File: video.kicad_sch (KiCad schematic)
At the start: 4 parts, among them J2 Board Interconnect Female, J2 Video Output Female, J3 Conn_02x08_Odd_Even

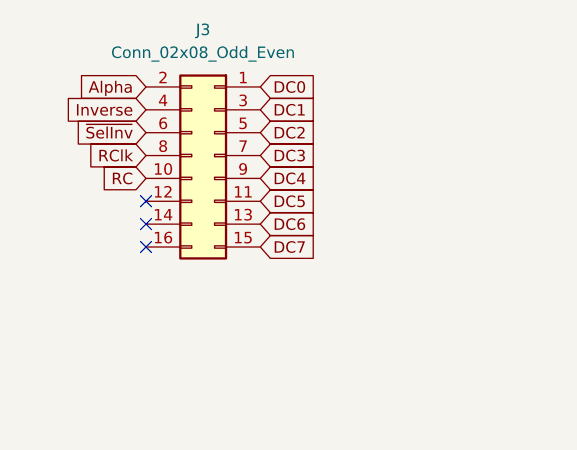
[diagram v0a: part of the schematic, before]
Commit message: reinforce power rails
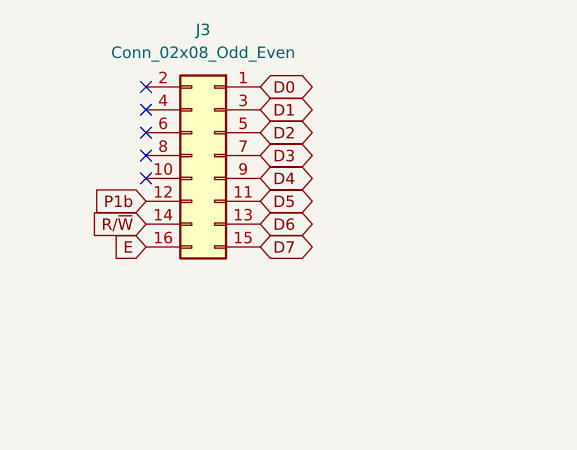
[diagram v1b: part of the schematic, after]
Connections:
- net P1b: now reaches J3.12 (Pin_12)
- net R/~{W}: now reaches J3.14 (Pin_14)
- net E: now reaches J3.16 (Pin_16)
- net Alpha: no longer names the net of J3.2 (Pin_2)
- net DC0 renamed D0
- net DC1 renamed D1
- net DC2 renamed D2
- net DC3 renamed D3
- net DC4 renamed D4
- net DC5 renamed D5
- net DC6 renamed D6
- net DC7 renamed D7
- net Inverse: no longer names the net of J3.4 (Pin_4)
- net RC: no longer names the net of J3.10 (Pin_10)
- net RClk: no longer names the net of J3.8 (Pin_8)
- net ~{SelInv}: no longer names the net of J3.6 (Pin_6)
- no-connect marks 5 -> 7
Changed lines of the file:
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@@
     (comment 2 "Reposition dram and buffer")
   )
-  (no_connect (at 123.19 116.84))
-  (no_connect (at 123.19 121.92))
-  (no_connect (at 123.19 119.38))
+  (no_connect (at 123.19 111.76))
+  (no_connect (at 123.19 114.3))
+  (no_connect (at 123.19 104.14))
+  (no_connect (at 123.19 106.68))
   (no_connect (at 137.1092 165.4048))
   (no_connect (at 124.4092 190.8048))
+  (no_connect (at 123.19 109.22))
   (global_label "DO5" (shape input) (at 124.4092 180.6448 180) (fields_autoplaced)
     (effects (font (size 1.27 1.27)) (justify right))
     (property "Intersheetrefs" "${INTERSHEET_REFS}" (at 118.3476 180.6448 0)
+      (effects (font (size 1.27 1.27)) (justify right) hide)
+    )
+  )
+  (global_label "D6" (shape bidirectional) (at 135.89 119.38 0) (fields_autoplaced)
+    (effects (font (size 1.27 1.27)) (justify left))
+    (property "Intersheetrefs" "${INTERSHEET_REFS}" (at 140.6937 119.3006 0)
+      (effects (font (size 1.27 1.27)) (justify left) hide)
+    )
+  )
+  (global_label "P1b" (shape input) (at 123.19 116.84 180) (fields_autoplaced)
+    (effects (font (size 1.27 1.27)) (justify right))
+    (property "Intersheetrefs" "${INTERSHEET_REFS}" (at 116.5763 116.84 0)
       (effects (font (size 1.27 1.27)) (justify right) hide)
     )
@@
     )
   )
+  (global_label "D5" (shape bidirectional) (at 135.89 116.84 0) (fields_autoplaced)
+    (effects (font (size 1.27 1.27)) (justify left))
+    (property "Intersheetrefs" "${INTERSHEET_REFS}" (at 140.6937 116.7606 0)
+      (effects (font (size 1.27 1.27)) (justify left) hide)
+    )
+  )
+  (global_label "D2" (shape bidirectional) (at 135.89 109.22 0) (fields_autoplaced)
+    (effects (font (size 1.27 1.27)) (justify left))
+    (property "Intersheetrefs" "${INTERSHEET_REFS}" (at 140.6937 109.1406 0)
+      (effects (font (size 1.27 1.27)) (justify left) hide)
+    )
+  )
+  (global_label "R{slash}~{W}" (shape input) (at 123.19 119.38 180) (fields_autoplaced)
+    (effects (font (size 1.27 1.27)) (justify right))
+    (property "Intersheetrefs" "${INTERSHEET_REFS}" (at 116.8071 119.38 0)
+      (effects (font (size 1.27 1.27)) (justify right) hide)
+    )
+  )
+  (global_label "D3" (shape bidirectional) (at 135.89 111.76 0) (fields_autoplaced)
+    (effects (font (size 1.27 1.27)) (justify left))
+    (property "Intersheetrefs" "${INTERSHEET_REFS}" (at 140.6937 111.6806 0)
+      (effects (font (size 1.27 1.27)) (justify left) hide)
+    )
+  )
   (global_label "SOUND" (shape input) (at 202.6412 138.5824 180) (fields_autoplaced)
     (effects (font (size 1.27 1.27)) (justify right))
     (property "Intersheetrefs" "${INTERSHEET_REFS}" (at 193.9186 138.5824 0)
       (effects (font (size 1.27 1.27)) (justify right) hide)
-    )
-  )
-  (global_label "DC3" (shape input) (at 135.89 111.76 0) (fields_autoplaced)
-    (effects (font (size 1.27 1.27)) (justify left))
-    (property "Intersheetrefs" "${INTERSHEET_REFS}" (at 142.5453 111.76 0)
-      (effects (font (size 1.27 1.27)) (justify left) hide)
-    )
-  )
-  (global_label "DC2" (shape input) (at 135.89 109.22 0) (fields_autoplaced)
-    (effects (font (size 1.27 1.27)) (justify left))
-    (property "Intersheetrefs" "${INTERSHEET_REFS}" (at 142.5453 109.22 0)
-      (effects (font (size 1.27 1.27)) (justify left) hide)
-    )
-  )
-  (global_label "DC7" (shape input) (at 135.89 121.92 0) (fields_autoplaced)
-    (effects (font (size 1.27 1.27)) (justify left))
-    (property "Intersheetrefs" "${INTERSHEET_REFS}" (at 142.5453 121.92 0)
-      (effects (font (size 1.27 1.27)) (justify left) hide)
-    )
-  )
-  (global_label "DC5" (shape input) (at 135.89 116.84 0) (fields_autoplaced)
-    (effects (font (size 1.27 1.27)) (justify left))
-    (property "Intersheetrefs" "${INTERSHEET_REFS}" (at 142.5453 116.84 0)
-      (effects (font (size 1.27 1.27)) (justify left) hide)
     )
   )
@@
     )
   )
-  (global_label "~{SelInv}" (shape input) (at 123.19 109.22 180) (fields_autoplaced)
-    (effects (font (size 1.27 1.27)) (justify right))
-    (property "Intersheetrefs" "${INTERSHEET_REFS}" (at 114.5201 109.22 0)
-      (effects (font (size 1.27 1.27)) (justify right) hide)
-    )
-  )
   (global_label "~{A}{slash}G" (shape input) (at 137.1092 188.2648 0) (fields_autoplaced)
     (effects (font (size 1.27 1.27)) (justify left))
@@
     )
   )
-  (global_label "DC6" (shape input) (at 135.89 119.38 0) (fields_autoplaced)
+  (global_label "D1" (shape bidirectional) (at 135.89 106.68 0) (fields_autoplaced)
     (effects (font (size 1.27 1.27)) (justify left))
-    (property "Intersheetrefs" "${INTERSHEET_REFS}" (at 142.5453 119.38 0)
+    (property "Intersheetrefs" "${INTERSHEET_REFS}" (at 140.6937 106.6006 0)
       (effects (font (size 1.27 1.27)) (justify left) hide)
     )
@@
     )
   )
-  (global_label "RClk" (shape input) (at 123.19 111.76 180) (fields_autoplaced)
-    (effects (font (size 1.27 1.27)) (justify right))
-    (property "Intersheetrefs" "${INTERSHEET_REFS}" (at 116.0509 111.76 0)
-      (effects (font (size 1.27 1.27)) (justify right) hide)
-    )
-  )
-  (global_label "DC0" (shape input) (at 135.89 104.14 0) (fields_autoplaced)
+  (global_label "D0" (shape bidirectional) (at 135.89 104.14 0) (fields_autoplaced)
     (effects (font (size 1.27 1.27)) (justify left))
-    (property "Intersheetrefs" "${INTERSHEET_REFS}" (at 142.5453 104.14 0)
+    (property "Intersheetrefs" "${INTERSHEET_REFS}" (at 140.6937 104.2194 0)
       (effects (font (size 1.27 1.27)) (justify left) hide)
     )
@@
     )
   )
-  (global_label "RC" (shape input) (at 123.19 114.3 180) (fields_autoplaced)
-    (effects (font (size 1.27 1.27)) (justify right))
-    (property "Intersheetrefs" "${INTERSHEET_REFS}" (at 117.7442 114.3 0)
-      (effects (font (size 1.27 1.27)) (justify right) hide)
-    )
-  )
   (global_label "VID OUT" (shape output) (at 167.64 171.45 0) (fields_autoplaced)
     (effects (font (size 1.27 1.27)) (justify left))
@@
     (property "Intersheetrefs" "${INTERSHEET_REFS}" (at 118.3476 185.7248 0)
       (effects (font (size 1.27 1.27)) (justify right) hide)
+    )
+  )
+  (global_label "D7" (shape bidirectional) (at 135.89 121.92 0) (fields_autoplaced)
+    (effects (font (size 1.27 1.27)) (justify left))
+    (property "Intersheetrefs" "${INTERSHEET_REFS}" (at 140.6937 121.8406 0)
+      (effects (font (size 1.27 1.27)) (justify left) hide)
     )
   )
@@
     )
   )
-  (global_label "DC1" (shape input) (at 135.89 106.68 0) (fields_autoplaced)
-    (effects (font (size 1.27 1.27)) (justify left))
-    (property "Intersheetrefs" "${INTERSHEET_REFS}" (at 142.5453 106.68 0)
-      (effects (font (size 1.27 1.27)) (justify left) hide)
-    )
-  )
-  (global_label "DC4" (shape input) (at 135.89 114.3 0) (fields_autoplaced)
-    (effects (font (size 1.27 1.27)) (justify left))
-    (property "Intersheetrefs" "${INTERSHEET_REFS}" (at 142.5453 114.3 0)
-      (effects (font (size 1.27 1.27)) (justify left) hide)
+  (global_label "E" (shape input) (at 123.19 121.92 180) (fields_autoplaced)
+    (effects (font (size 1.27 1.27)) (justify right))
+    (property "Intersheetrefs" "${INTERSHEET_REFS}" (at 119.7168 121.8406 0)
+      (effects (font (size 1.27 1.27)) (justify right) hide)
     )
   )
@@
     )
   )
-  (global_label "Inverse" (shape input) (at 123.19 106.68 180) (fields_autoplaced)
-    (effects (font (size 1.27 1.27)) (justify right))
-    (property "Intersheetrefs" "${INTERSHEET_REFS}" (at 113.4919 106.68 0)
-      (effects (font (size 1.27 1.27)) (justify right) hide)
+  (global_label "D4" (shape bidirectional) (at 135.89 114.3 0) (fields_autoplaced)
+    (effects (font (size 1.27 1.27)) (justify left))
+    (property "Intersheetrefs" "${INTERSHEET_REFS}" (at 140.6937 114.2206 0)
+      (effects (font (size 1.27 1.27)) (justify left) hide)
     )
   )
-  (global_label "Alpha" (shape input) (at 123.19 104.14 180) (fields_autoplaced)
-    (effects (font (size 1.27 1.27)) (justify right))
-    (property "Intersheetrefs" "${INTERSHEET_REFS}" (at 115.004 104.14 0)
-      (effects (font (size 1.27 1.27)) (justify right) hide)
-    )
-  )

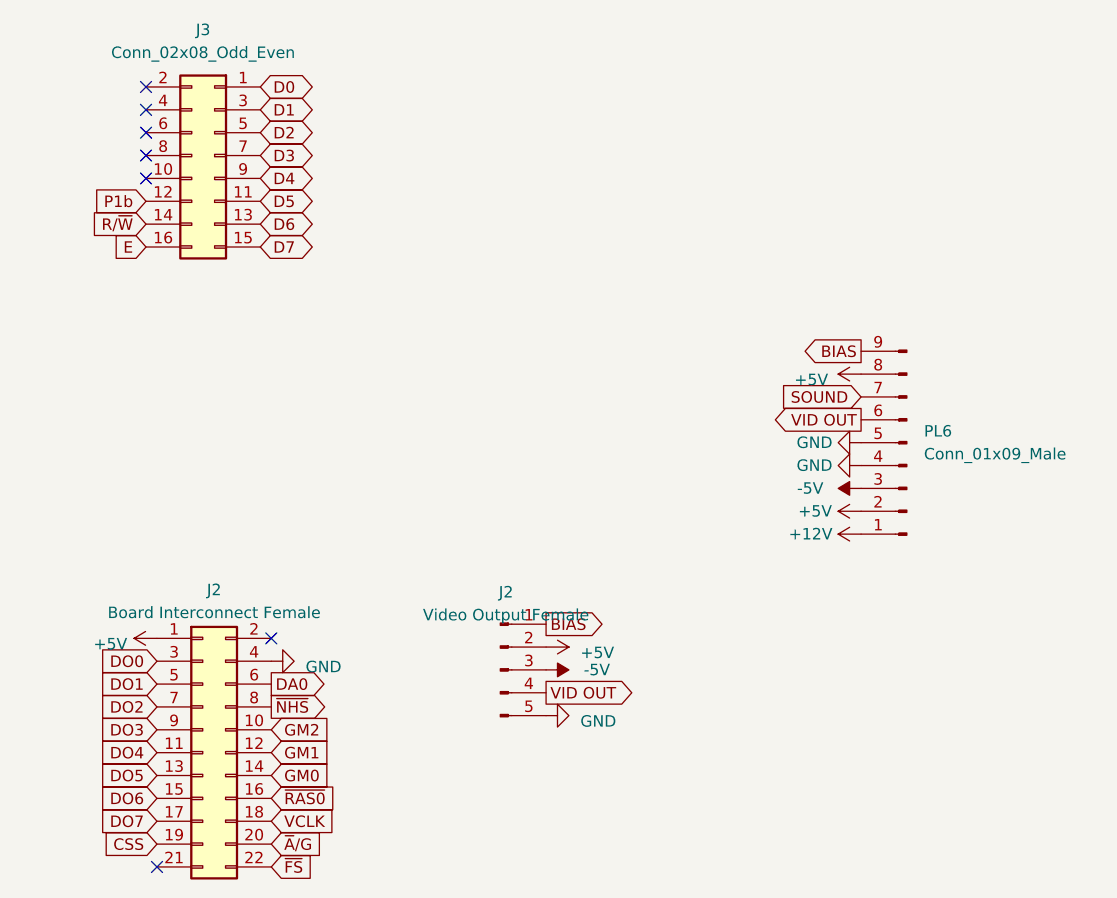
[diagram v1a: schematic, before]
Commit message: reinforce audio traces
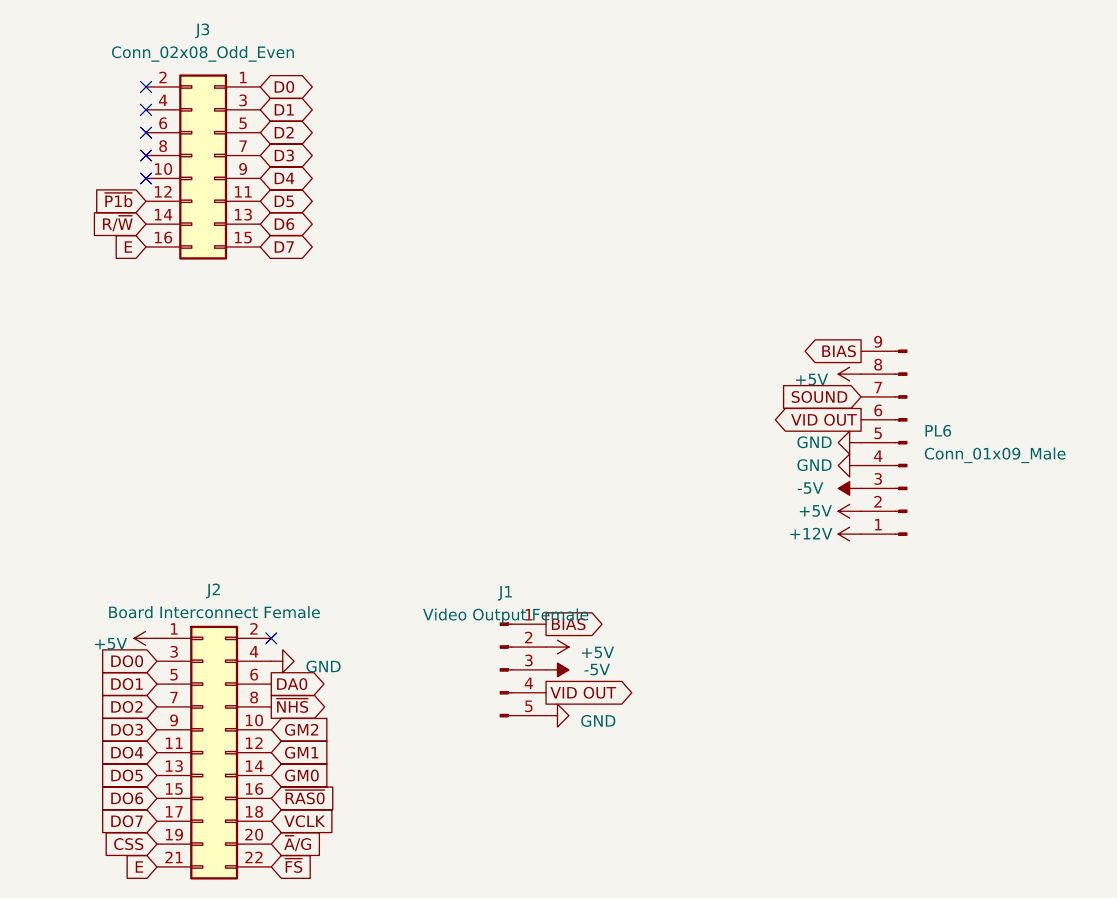
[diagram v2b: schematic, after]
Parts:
- renumbered J2 to J1
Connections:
- net E: now also J2.21 (Pin_21)
- net P1b renamed ~{P1b}
- no-connect marks 7 -> 6
